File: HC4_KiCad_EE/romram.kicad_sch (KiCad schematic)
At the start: 5 parts, among them J1 Conn_02x04_Odd_Even, J4 UPDI_and_Debug, U1 ATmega4809-A

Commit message: 基板に反映
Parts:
- added J5: Expantion, Connector_PinHeader_2.54mm:PinHeader_2x06_P2.54mm_Vertical, symbol Connector_Generic:Conn_02x06_Odd_Even
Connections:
- net DBus_A0: now also J5.10 (Pin_10)
- net DBus_A1: now also J5.8 (Pin_8)
- net DBus_A2: now also J5.6 (Pin_6)
- net DBus_A3: now also J5.4 (Pin_4)
- net DBus_D0: now also J5.9 (Pin_9)
- net DBus_D1: now also J5.7 (Pin_7)
- net DBus_D2: now also J5.5 (Pin_5)
- net DBus_D3: now also J5.3 (Pin_3)
- net GND: now also J5.2 (Pin_2)
- net VCC: now also J5.1 (Pin_1)
- net ~{RD}: now also J5.11 (Pin_11)
- net ~{WR}: now also J5.12 (Pin_12)

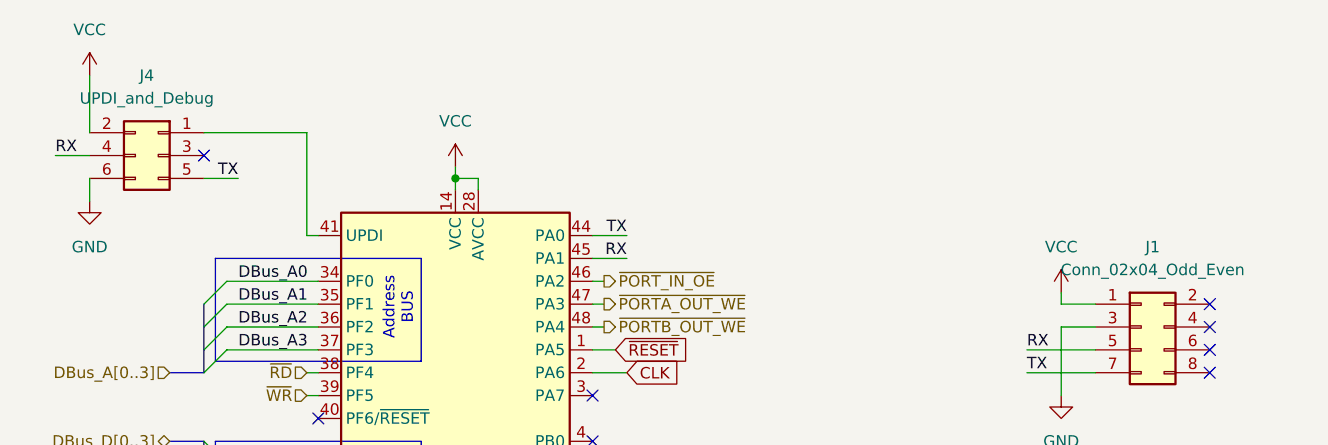
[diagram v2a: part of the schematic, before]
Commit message: feat:HC4e改版,BOMを令和最新版に更新,KiCadを10に更新
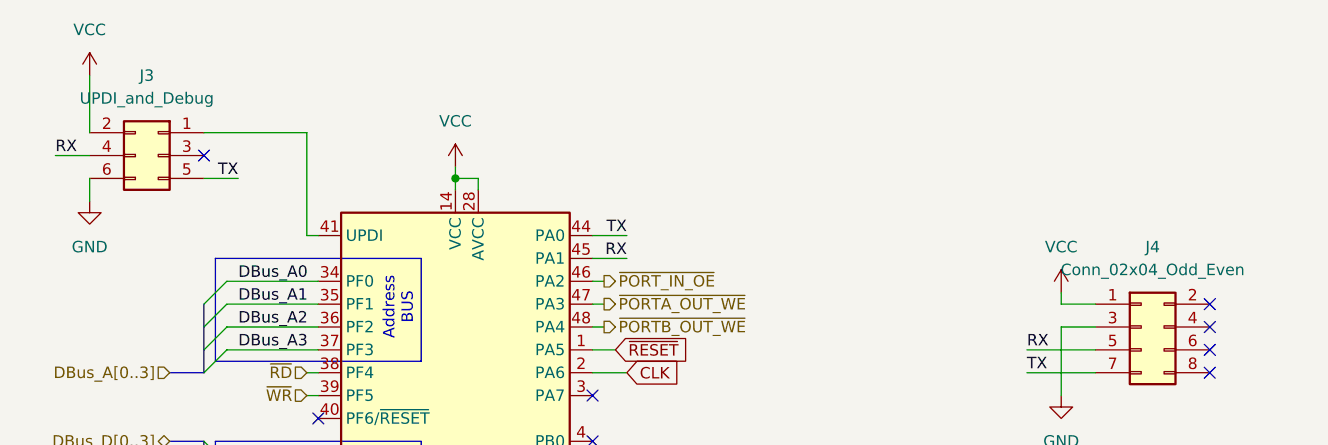
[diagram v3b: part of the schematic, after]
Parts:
- renumbered J4 to J3, J1 to J4

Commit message: 基板を若干改版、フットプリントの指定が外れていたのを修正
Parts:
- C2, C3: LCSC PN (none) -> C14663
- U1: LCSC PN (none) -> C1340574
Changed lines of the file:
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@@
+			)
+		)
+		(property "LCSC PN" "C14663"
+			(at 106.68 163.83 0)
+			(hide yes)
+			(show_name no)
+			(do_not_autoplace no)
+			(effects
+				(font
+					(size 1.27 1.27)
+				)
 			)
 		)
@@
 			)
 		)
+		(property "LCSC PN" ""
+			(at 52.07 68.58 0)
+			(hide yes)
+			(show_name no)
+			(do_not_autoplace no)
+			(effects
+				(font
+					(size 1.27 1.27)
+				)
+			)
+		)
 		(pin "6"
 		)
@@
 			)
 		)
+		(property "LCSC PN" ""
+			(at 161.29 87.63 0)
+			(hide yes)
+			(show_name no)
+			(do_not_autoplace no)
+			(effects
+				(font
+					(size 1.27 1.27)
+				)
+			)
+		)
 		(pin "1"
 		)
@@
 			)
 		)
+		(property "LCSC PN" "C14663"
+			(at 119.38 163.83 0)
+			(hide yes)
+			(show_name no)
+			(do_not_autoplace no)
+			(effects
+				(font
+					(size 1.27 1.27)
+				)
+			)
+		)
 		(pin "2"
 		)
@@
 			)
 		)
+		(property "LCSC PN" "C1340574"
+			(at 85.09 107.95 0)
+			(hide yes)
+			(show_name no)
+			(do_not_autoplace no)
+			(effects
+				(font
+					(size 1.27 1.27)
+				)
+			)
+		)
 		(pin "32"
 		)
@@
 			(at 167.64 137.16 0)
 			(hide yes)
+			(show_name no)
+			(do_not_autoplace no)
+			(effects
+				(font
+					(size 1.27 1.27)
+				)
+			)
+		)
+		(property "LCSC PN" ""
+			(at 167.64 137.16 0)
+			(hide yes)

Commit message: HC4eRev2完成
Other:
- company: (none) -> Dengiken
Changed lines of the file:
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@@
 	(title_block
 		(title "HC4e_CPU")
-		(date "2026-03-19")
+		(date "2026-05-23")
 		(rev "2.0")
+		(company "Dengiken")
 	)
 	(rectangle
@@
 		)
 	)
-	(embedded_fonts no)
 )
